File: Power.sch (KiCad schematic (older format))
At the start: 12 parts, among them CON1 DC 9V, SW1 POWER SW, U1 LM7805CT

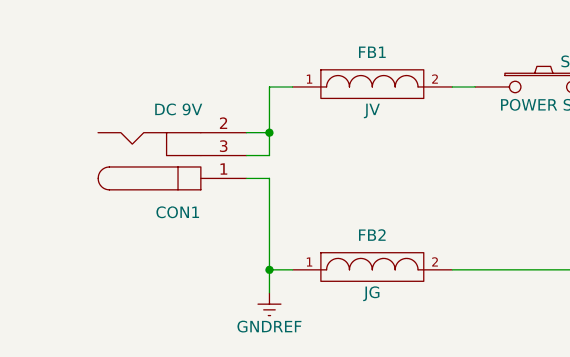
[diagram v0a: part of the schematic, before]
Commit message: Cartridge and card slots
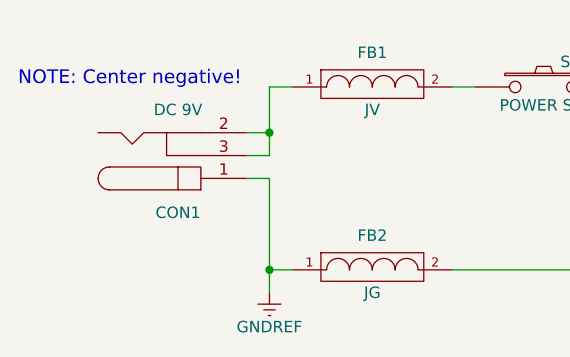
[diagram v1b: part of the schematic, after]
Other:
- note added: "NOTE: Center negative!"
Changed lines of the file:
@@
 LIBS:contrib
 LIBS:valves
-LIBS:SMS_Chips
+LIBS:SMSSchematic-cache
 EELAYER 25 0
 EELAYER END
@@
 	4300 1900 4300 2500
 $Comp
-L GNDPWR #PWR019
+L GNDPWR #PWR021
 U 1 1 56963B5D
 P 4300 2500
-F 0 "#PWR019" H 4300 2300 50  0001 C CNN
+F 0 "#PWR021" H 4300 2300 50  0001 C CNN
 F 1 "GNDPWR" H 4300 2370 50  0000 C CNN
 F 2 "" H 4300 2450 50  0000 C CNN
@@
 Connection ~ 4300 2400
 $Comp
-L GNDREF #PWR020
+L GNDREF #PWR022
 U 1 1 56963B9D
 P 1800 2500
-F 0 "#PWR020" H 1800 2250 50  0001 C CNN
+F 0 "#PWR022" H 1800 2250 50  0001 C CNN
 F 1 "GNDREF" H 1800 2350 50  0000 C CNN
 F 2 "" H 1800 2500 50  0000 C CNN
@@
 	5600 2400 5600 2200
 $Comp
-L VCC #PWR021
+L VCC #PWR023
 U 1 1 56963E24
 P 5600 1500
-F 0 "#PWR021" H 5600 1350 50  0001 C CNN
+F 0 "#PWR023" H 5600 1350 50  0001 C CNN
 F 1 "VCC" H 5600 1650 50  0000 C CNN
 F 2 "" H 5600 1500 50  0000 C CNN
@@
 	1    0    0    -1
 $EndComp
+Text Notes 700  1600 0    60   ~ 0
+NOTE: Center negative!
 $EndSCHEMATC
